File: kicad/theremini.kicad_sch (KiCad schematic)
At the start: 2 parts, among them U1 VL53L0CXV0DH/1, U2 VL53L0CXV0DH/1

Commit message: Add libraries
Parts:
- removed U1: VL53L0CXV0DH/1, VL53L0CXV0DH1:OPTO-SMD_12P_VL53L0CXV0DH-1, symbol VL53L0CXV0DH/1:VL53L0CXV0DH/1
- added U1: NAU88C22YG, NAU88C22YG:QFN-32_L5.0-W5.0-P0.50-BL-EP3.4, symbol NAU88C22YG:NAU88C22YG
- added U3: STM32L432KBUx, Package_DFN_QFN:QFN-32-1EP_5x5mm_P0.5mm_EP3.45x3.45mm, symbol MCU_ST_STM32L4:STM32L432KBUx
- added U4: VL53L0CXV0DH/1, VL53L0CXV0DH1:OPTO-SMD_12P_VL53L0CXV0DH-1, symbol VL53L0CXV0DH/1:VL53L0CXV0DH/1
- added U5: KLJ-01304T-08R07W, KLJ-01304T-08R07W:BUZ-SMD_4P-L13.0-W13.0-P11.4-BL, symbol KLJ-01304T-08R07W:KLJ-01304T-08R07W
- added U6: PJ-327C-4A, PJ-327C-4A:AUDIO-SMD_PJ-327C-4A, symbol PJ-327C-4A:PJ-327C-4A
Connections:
- new net: U3.16 (VSS), U3.32 (VSS), U3.33 (VSS)

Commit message: added things
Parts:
- removed U3: STM32L432KBUx, Package_DFN_QFN:QFN-32-1EP_5x5mm_P0.5mm_EP3.45x3.45mm, symbol MCU_ST_STM32L4:STM32L432KBUx
- added BT1: Battery, symbol Device:Battery
- added D1, D2: D_Schottky, symbol Device:D_Schottky
- added J1: USB_C_Receptacle_PowerOnly_6P, symbol Connector:USB_C_Receptacle_PowerOnly_6P
- added U7: STM32L432KBU6TR, STM32L432KBU6TR:UFQFPN-32_L5.0-W5.0-P0.50-TL-EP3.5, symbol STM32L432KBU6TR:STM32L432KBU6TR
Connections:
- new net: D2.2 (A), J1.A9 (VBUS), J1.B9 (VBUS)
- new net: BT1.1 (+), D1.2 (A)
- new net BUCK CONVERTER IN: D1.1 (K), D2.1 (K)
- new net GND: BT1.2 (-), J1.A12 (GND), J1.B12 (GND)

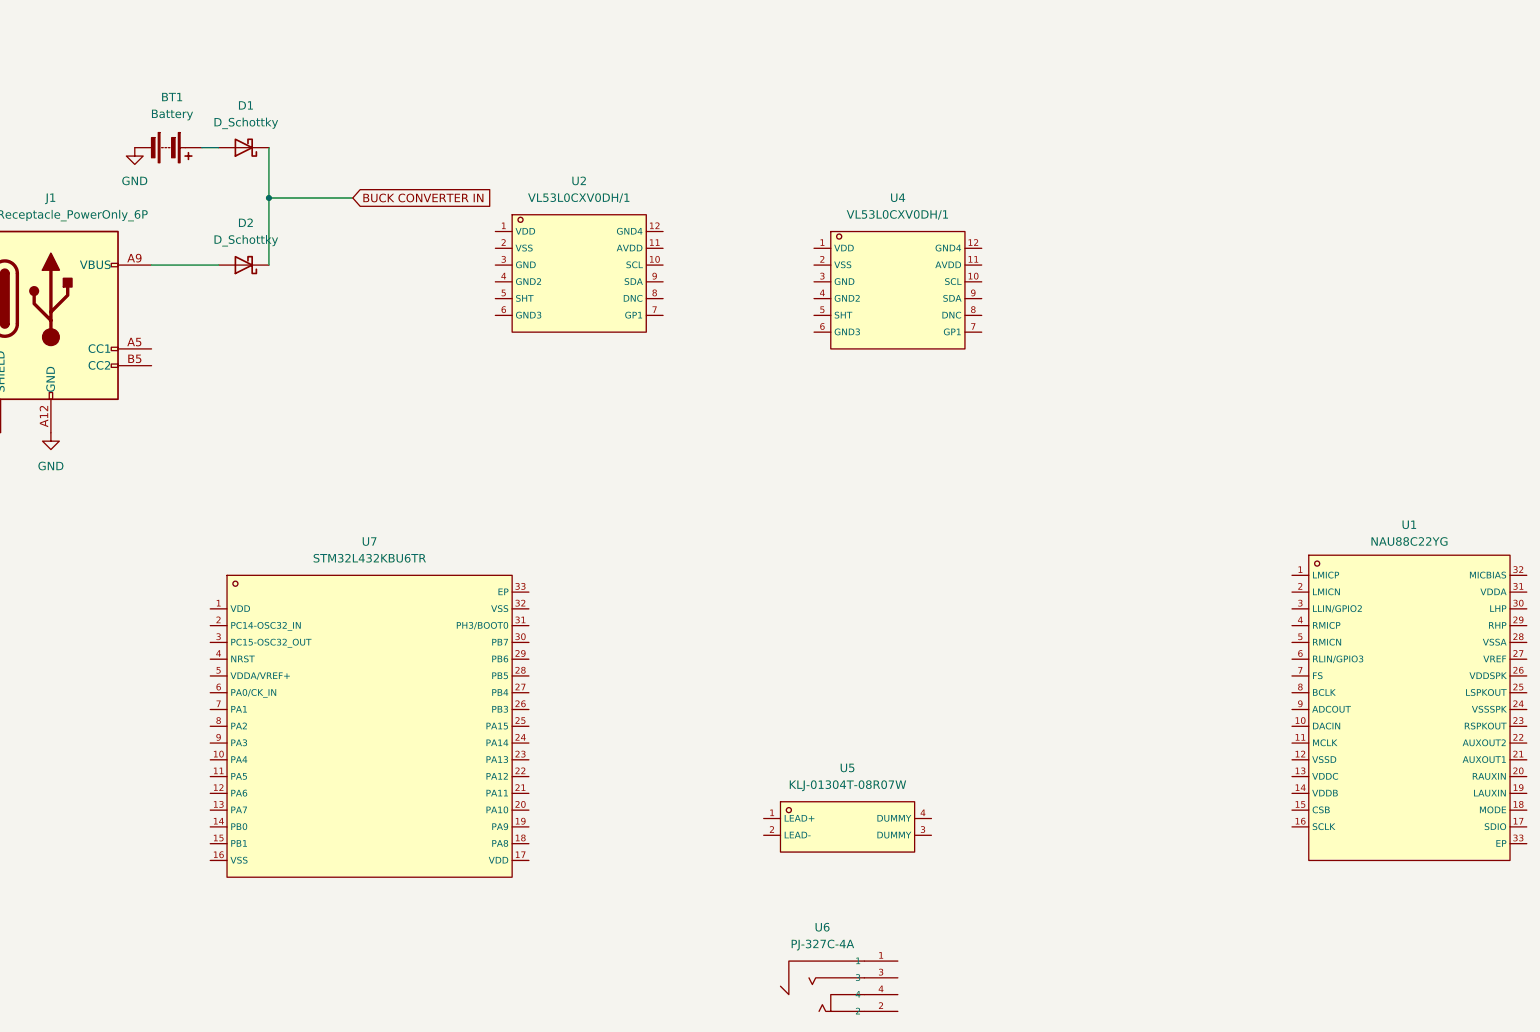
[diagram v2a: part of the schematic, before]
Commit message: Arrange library
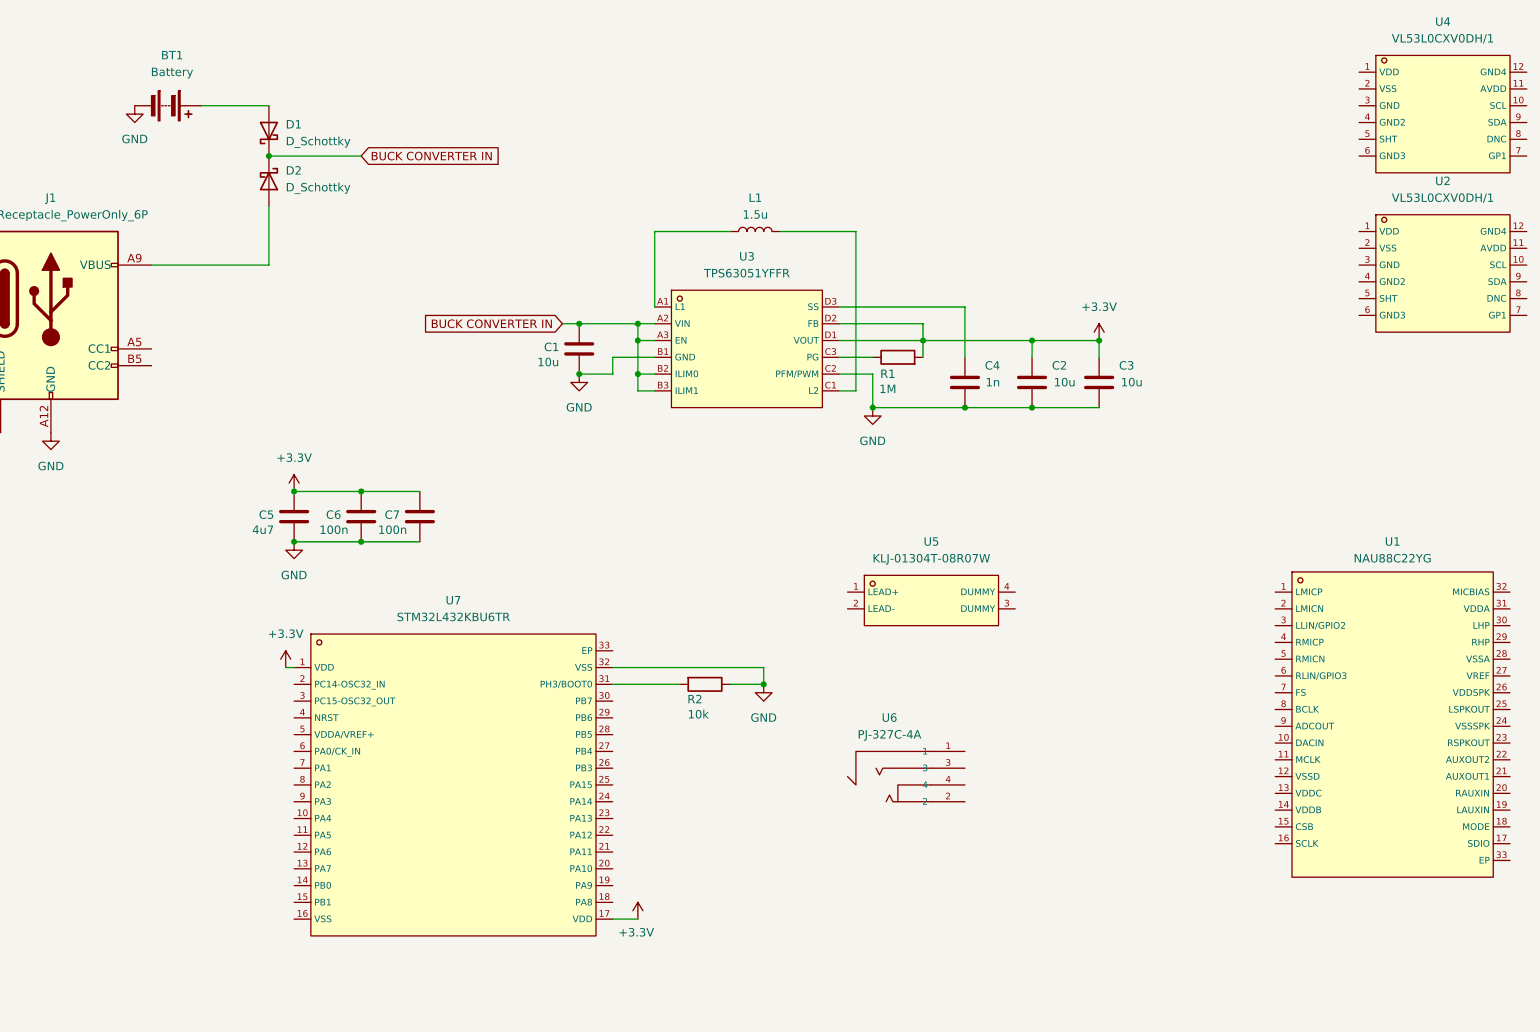
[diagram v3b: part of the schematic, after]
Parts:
- added C1, C2, C3: 10u, Capacitor_SMD:C_0603_1608Metric, symbol Device:C
- added C4: 1n, Capacitor_SMD:C_0603_1608Metric, symbol Device:C
- added C5: 4u7, Capacitor_SMD:C_0603_1608Metric, symbol Device:C
- added C6, C7: 100n, Capacitor_SMD:C_0603_1608Metric, symbol Device:C
- added L1: 1.5u, Inductor_SMD:L_0201_0603Metric, symbol Device:L
- added R1: 1M, Resistor_SMD:R_0201_0603Metric, symbol Device:R
- added R2: 10k, Resistor_SMD:R_0201_0603Metric, symbol Device:R
- added U3: TPS63051YFFR, TPS63051YFFR:DSBGA-12_L1.6-W1.2-R3-C4-P0.40-BL, symbol TPS63051YFFR:TPS63051YFFR
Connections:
- net BUCK CONVERTER IN: now also C1.1, U3.A2 (VIN), U3.A3 (EN), U3.B2 (ILIM0), U3.B3 (ILIM1)
- net GND: now also U7.32 (VSS), C1.2, C2.1, C3.1, C4.1, C5.2, C6.2, C7.2, R2.1, U3.B1 (GND), U3.C2 (PFM/PWM)
- net +3.3V: now reaches U7.1 (VDD)
- net +3.3V: now also U7.17 (VDD), C2.2, C3.2, C5.1, C6.1, C7.1, R1.2, U3.D1 (VOUT), U3.D2 (FB)
- net at U7.31 (PH3/BOOT0): now also R2.2
- new net: C4.2, U3.D3 (SS)
- new net: L1.1, U3.A1 (L1)
- new net: L1.2, U3.C1 (L2)
- new net: R1.1, U3.C3 (PG)
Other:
- moved on the sheet: BT1, D1, D2, U1, U2, U4, U5, U6, U7

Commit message: Connected things
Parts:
- removed J1: USB_C_Receptacle_PowerOnly_6P, symbol Connector:USB_C_Receptacle_PowerOnly_6P
- added C10, C11: 100n, Capacitor_SMD:C_0402_1005Metric, symbol Device:C
- added C12: 15p, Capacitor_SMD:C_0402_1005Metric, symbol Device:C
- added C8: 10n, Capacitor_SMD:C_0402_1005Metric, symbol Device:C
- added C9: 1u, Capacitor_SMD:C_0402_1005Metric, symbol Device:C
- added L2: BLM15AG601SN1D, BLM15AG601SN1D:L0402, symbol BLM15AG601SN1D:BLM15AG601SN1D
- added SW1: K2-1157SP-I4SW-04, BLM15AG601SN1D:SW-SMD_4P-L6.2-W6.2-P4.50-LS8.6, symbol K2-1157SP-I4SW-04:K2-1157SP-I4SW-04
- added U8: YTS1C0033BBG01, footprint:SW-SMD_YIYUAN_YTS1C003XXX, symbol YTS1C0033BBG01:YTS1C0033BBG01
- added U9: TYPE-C16PIN, TYPE-C16PIN:USB-C-SMD_TYPE-C16PIN, symbol TYPE-C16PIN:TYPE-C16PIN
- added X1: OT32258MJBA4SL, OT32258MJBA4SL:OSC-SMD_4P-L3.2-W2.5-BL, symbol OT32258MJBA4SL:OT32258MJBA4SL
- C1, C2, C3, C4, C5, C6, C7: footprint Capacitor_SMD:C_0603_1608Metric -> Capacitor_SMD:C_0402_1005Metric
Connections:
- net +3.3V: now also C11.1, L2.1, X1.1 (Tri-state), X1.4 (VDD)
- net GND: now also C10.2, C11.2, C12.2, C8.2, C9.2, U8.1, U8.3, U8.4, U9.1 (SHELL), U9.2 (SHELL), U9.3 (SHELL), U9.4 (SHELL), U9.A1B12 (GND), U9.B1A12 (GND), X1.2 (GND)
- net at D2.2 (A): now also U9.A4B9 (VBUS), U9.B4A9 (VBUS)
- net NRST: now reaches U7.4 (NRST)
- net NRST: now also C10.1, U8.2
- net VDDA: now reaches U7.5 (VDDA/VREF+)
- net VDDA: now also C8.1, C9.1, L2.2
- net XTAL OUT: now reaches U7.6 (PA0/CK_IN)
- net XTAL OUT: now also C12.1, X1.3 (OUTPUT)
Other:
- moved on the sheet: C1, C2, C3, C4, C5, C6, C7, L1, R1, R2, U1, U2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

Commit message: just update ig
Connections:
- net GND: now also R2.2; no longer R2.1
- net BOOT0: now reaches U7.31 (PH3/BOOT0)
- net BOOT0: now also R2.1; no longer R2.2
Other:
- moved on the sheet: C11, R2, U1

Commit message: just commit
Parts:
- removed U3: TPS63051YFFR, TPS63051YFFR:DSBGA-12_L1.6-W1.2-R3-C4-P0.40-BL, symbol TPS63051YFFR:TPS63051YFFR
- added U10: TPS63051RMWR, TPS63051RMWR:QFN-12_L2.5-W2.5-P0.50-TL, symbol TPS63051RMWR:TPS63051RMWR
- L1: footprint Inductor_SMD:L_0201_0603Metric -> Inductor_SMD:L_0603_1608Metric
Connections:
- net +3.3V: now also U10.4 (VOUT), U10.5 (FB)
- net BUCK CONVERTER IN: now also U10.10 (ILIM0), U10.11 (EN), U10.12 (VIN)
- net GND: now also U10.2 (GND), U10.6 (PFM/PWM), U10.9 (GND)
- net at C4.2: now also U10.7 (SS)
- net I2S_SCK: now reaches U7.18 (PA8)
- net I2S_FS: now reaches U7.19 (PA9)
- net I2S_SD: now reaches U7.20 (PA10)
- net SCL: now reaches U7.29 (PB6)
- net SDA: now reaches U7.30 (PB7)
- net at L1.1: now also U10.3 (L2)
- net at L1.2: now also U10.1 (L1)
- net at R1.1: now also U10.8 (PG)
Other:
- moved on the sheet: C1, C2, C3, C4, C5, C6, C7, L1, R1, R2

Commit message: quick quick quiiick
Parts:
- added C13, C14, C15: 1u, Capacitor_SMD:C_0402_1005Metric, symbol Device:C
- added C16, C17, C18, C19: 4.7u, Capacitor_SMD:C_0402_1005Metric, symbol Device:C
- added R3, R4, R5: 10k, Resistor_SMD:R_0201_0603Metric, symbol Device:R
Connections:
- net +3.3V: now also U1.13 (VDDC), U1.14 (VDDB), U1.26 (VDDSPK), U1.31 (VDDA), C16.1, C17.1, C18.1, C19.1, R3.2
- net GND: now also U5.3 (DUMMY), U5.4 (DUMMY), U6.1, C16.2, C17.2, C18.2, C19.2
- net at U5.1 (LEAD+): now also C15.2
- net at U5.2 (LEAD-): now also U1.24 (VSSSPK)
- net at U6.2: now also C14.2
- net at U6.3: now also C13.1
- net JACK_DETECT: now reaches U6.4
- net JACK_DETECT: now also R3.1
- net at U1.23 (RSPKOUT): now also R5.2
- net at U1.25 (LSPKOUT): now also R4.2
- net at U1.29 (RHP): now also C13.2
- net at U1.30 (LHP): now also C14.1
- new net: C15.1, R4.1, R5.1
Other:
- moved on the sheet: U1, U5, U6
